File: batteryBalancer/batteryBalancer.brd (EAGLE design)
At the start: 103.5 x 94 mm, 15 parts

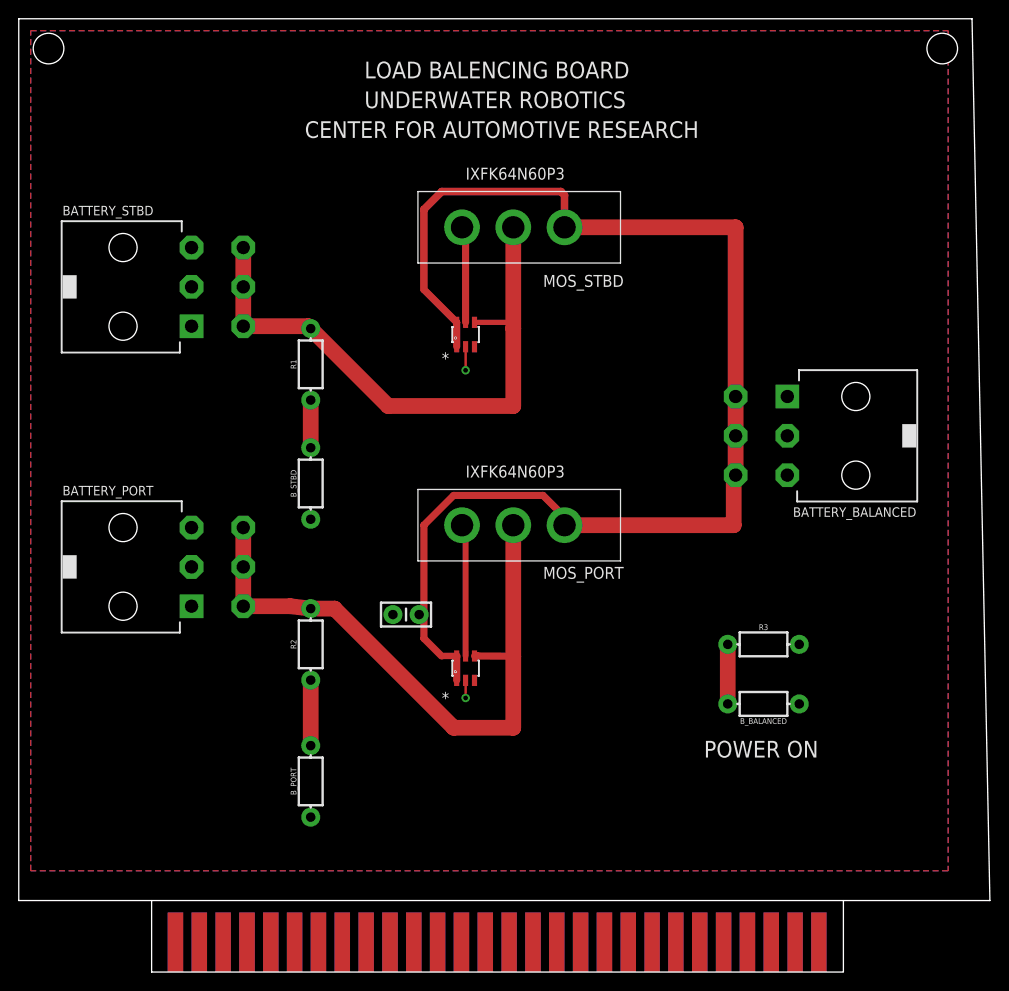
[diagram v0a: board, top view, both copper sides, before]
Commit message: Edgefinger not connected
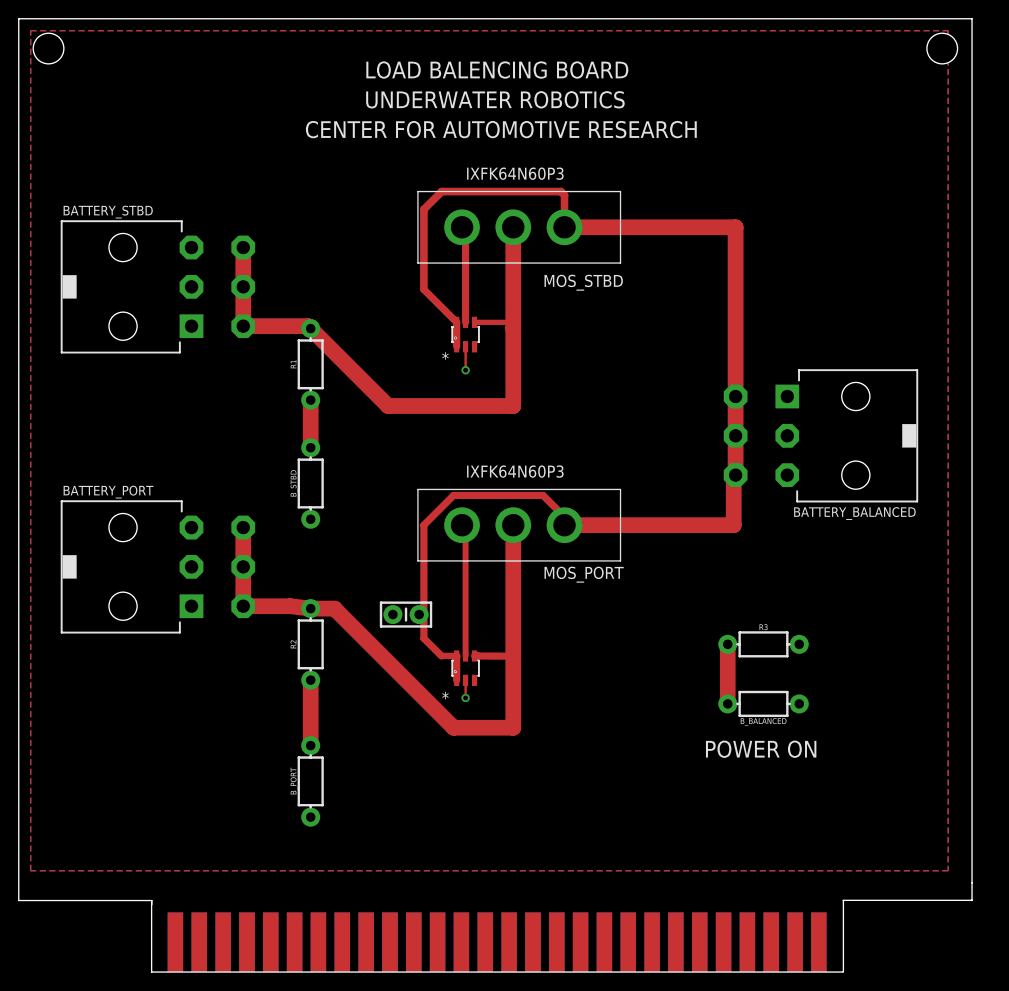
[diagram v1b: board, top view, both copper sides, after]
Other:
- board size 103.5 x 94 mm -> 101.6 x 94.4 mm
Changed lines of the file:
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@@
 <setting verticaltext="up"/>
 </settings>
-<grid distance="0.025" unitdist="inch" unit="inch" style="lines" multiple="1" display="no" altdistance="0.025" altunitdist="inch" altunit="inch"/>
+<grid distance="0.001" unitdist="inch" unit="inch" style="lines" multiple="1" display="no" altdistance="0.025" altunitdist="inch" altunit="inch"/>
 <layers>
 <layer number="1" name="Top" color="4" fill="1" visible="yes" active="yes"/>
@@
 <board>
 <plain>
-<wire x1="0" y1="7.62" x2="103.505" y2="7.62" width="0" layer="20"/>
-<wire x1="103.505" y1="7.62" x2="101.6" y2="101.6" width="0" layer="20"/>
+<wire x1="101.6" y1="7.62" x2="101.6" y2="7.6454" width="0" layer="20"/>
+<wire x1="101.6" y1="9.4996" x2="101.6" y2="101.6" width="0" layer="20"/>
 <wire x1="101.6" y1="101.6" x2="0" y2="101.6" width="0" layer="20"/>
 <wire x1="0" y1="101.6" x2="0" y2="7.62" width="0" layer="20"/>
@@
 <text x="45.085" y="64.77" size="1.27" layer="21">*</text>
 <text x="45.085" y="28.575" size="1.27" layer="21">*</text>
+<wire x1="14.1732" y1="7.62" x2="0" y2="7.62" width="0" layer="20"/>
+<wire x1="14.1732" y1="7.62" x2="14.1732" y2="7.1882" width="0" layer="20"/>
+<wire x1="87.8586" y1="7.6454" x2="101.6" y2="7.6454" width="0" layer="20"/>
+<wire x1="101.6" y1="7.6454" x2="101.6" y2="9.4996" width="0" layer="20"/>
 </plain>
 <attributes>
